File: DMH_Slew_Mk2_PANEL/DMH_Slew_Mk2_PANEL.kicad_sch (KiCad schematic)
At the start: 30 parts, among them J0 Panel_GND_Solder_Wire_Pad

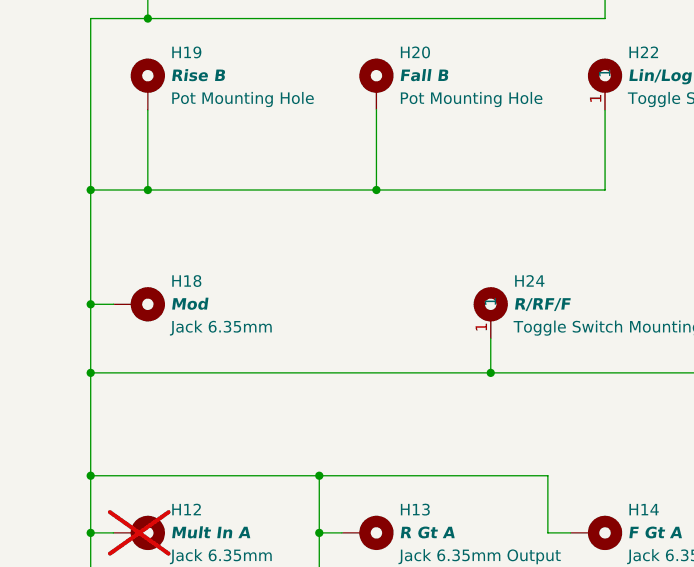
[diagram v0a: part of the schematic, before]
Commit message: Designed Controls PCB
... and removed Mod feature
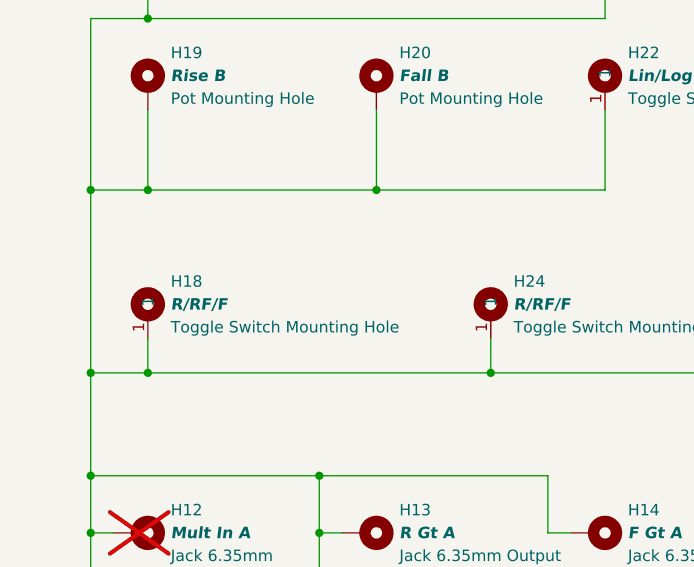
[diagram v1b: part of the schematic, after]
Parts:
- removed H18: Mod, SynthStuff:Jack_6.35mm_Cutout_v3, symbol SynthStuff:MountingHole_Jack6.35mm_v2
- added H18: R/RF/F, SynthStuff:Toggle_Switch_TE_Cutout, symbol SynthStuff:MountingHole_ToggleSwitch
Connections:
- net GND: now also H18.1
